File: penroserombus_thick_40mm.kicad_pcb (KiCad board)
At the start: 2 copper layers, 52.4 x 38 mm, 13 parts, among them J1 Conn_01x03_Female, J2 Conn_01x03_Female, J3 Conn_01x03_Male, J4 Conn_01x03_Male, SW1 SW_DPDT_x2

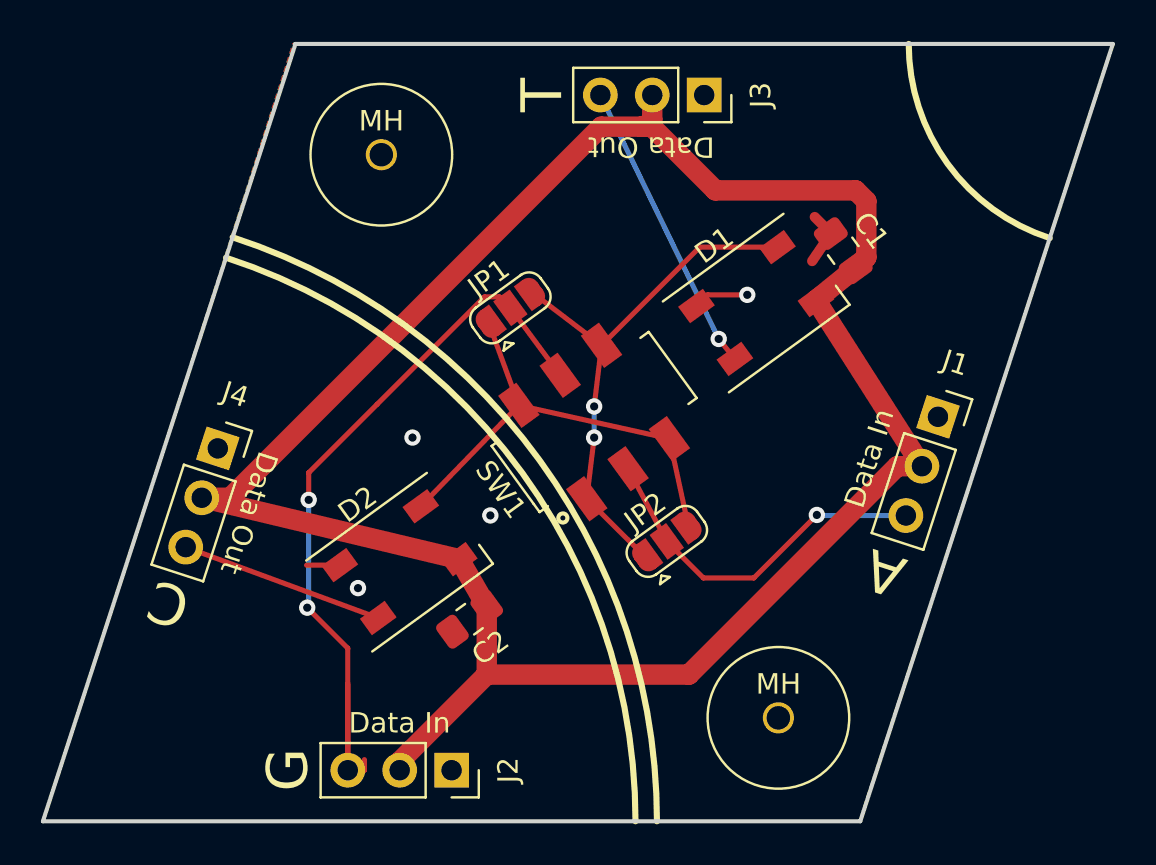
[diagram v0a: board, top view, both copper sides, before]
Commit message: added more mounting holes and generated gerbers
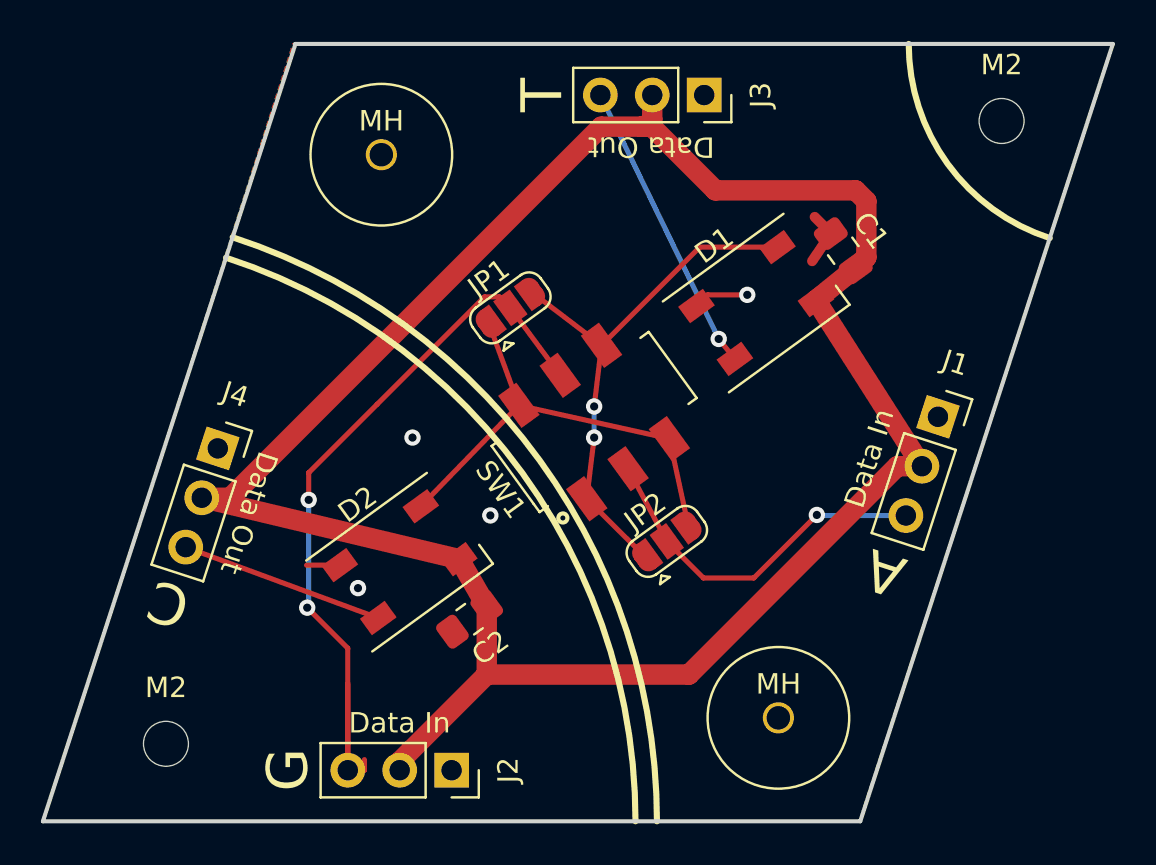
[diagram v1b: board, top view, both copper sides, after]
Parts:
- added M2: MountingHole_2.2mm_M2_ISO7380, MountingHole:MountingHole_2.2mm_M2_ISO7380, F.Cu at (126.9, 110.2)
- added M2: MountingHole_2.2mm_M2_ISO7380, MountingHole:MountingHole_2.2mm_M2_ISO7380, F.Cu at (167.8, 79.8)

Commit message: board has 4 leds instead of 2.
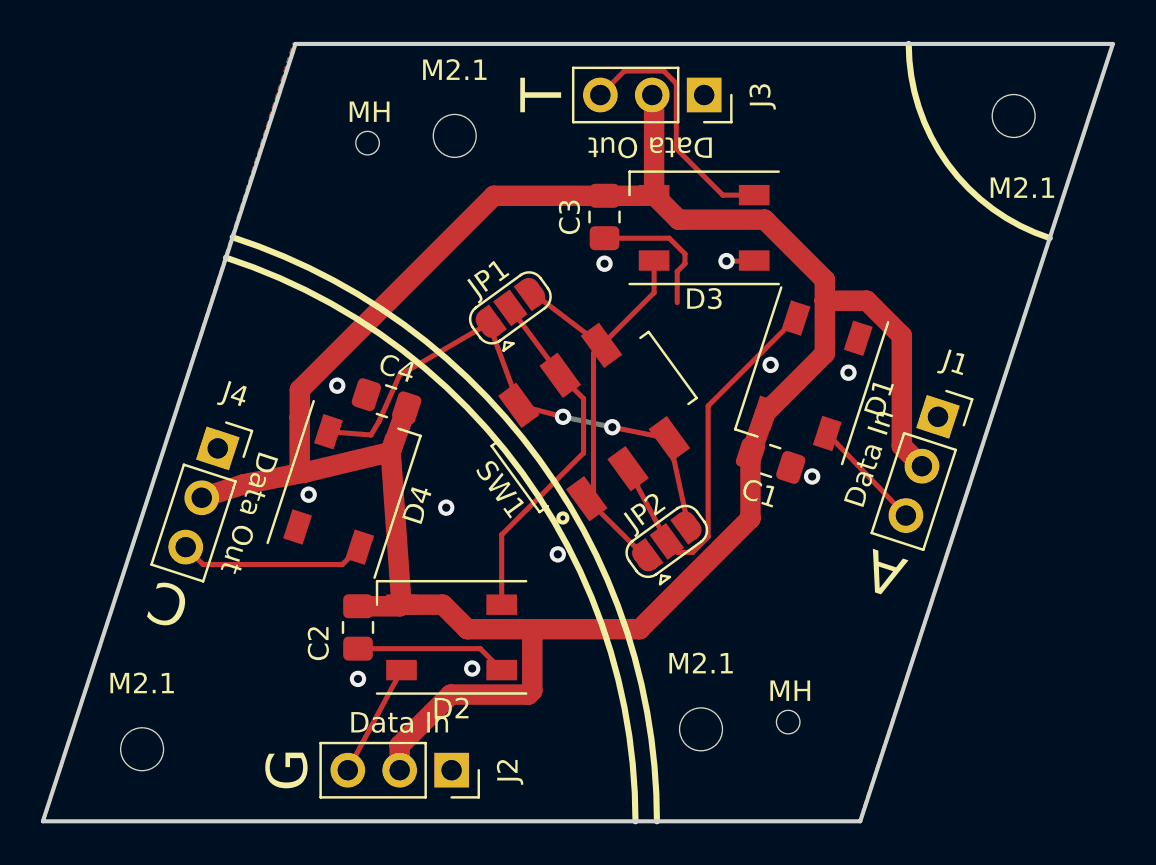
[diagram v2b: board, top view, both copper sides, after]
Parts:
- removed M2 (x2): MountingHole_2.2mm_M2_ISO7380, MountingHole:MountingHole_2.2mm_M2_ISO7380
- removed the MH at (156.8, 109.0)
- removed the MH at (137.4, 81.4)
- added C3: C, Capacitor_SMD:C_0805_2012Metric_Pad1.18x1.45mm_HandSolder, F.Cu at (148.3, 84.5)
- added C4: C, Capacitor_SMD:C_0805_2012Metric_Pad1.18x1.45mm_HandSolder, F.Cu at (137.7, 93.5)
- added D3: SK6812, LED_SMD:LED_SK6812_PLCC4_5.0x5.0mm_P3.2mm, F.Cu at (153.2, 85.0)
- added D4: SK6812, LED_SMD:LED_SK6812_PLCC4_5.0x5.0mm_P3.2mm, F.Cu at (135.6, 97.8)
- added M2.1: MountingHole_2.1mm, MountingHole:MountingHole_2.1mm, F.Cu at (141.0, 80.5)
- added M2.1: MountingHole_2.1mm, MountingHole:MountingHole_2.1mm, F.Cu at (168.4, 79.5)
- added M2.1: MountingHole_2.1mm, MountingHole:MountingHole_2.1mm, F.Cu at (153.1, 109.5)
- added M2.1: MountingHole_2.1mm, MountingHole:MountingHole_2.1mm, F.Cu at (125.7, 110.5)
- added MH: Pushpin_mountinghole, penroserombus:Pushpin_mountinghole, F.Cu at (157.3, 109.2)
- added MH: Pushpin_mountinghole, penroserombus:Pushpin_mountinghole, F.Cu at (136.7, 80.8)
- moved C1 10.9 mm to (156.5, 96.4), turned to 162 degrees
- moved C2 5.48 mm to (136.3, 104.5), turned to 90 degrees
- moved D1 4.48 mm to (158.5, 92.2), turned to 252 degrees
- moved D2 4.48 mm to (140.9, 105.0), turned to 180 degrees
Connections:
- J1 pad 3: Net-(J1-Pad3) -> Net-(D1-Pad2)
- J2 pad 3: Net-(J2-Pad3) -> Net-(D2-Pad2)
- J3 pad 3: Net-(D1-Pad4) -> Net-(D3-Pad4)
- J4 pad 3: Net-(D2-Pad4) -> Net-(D4-Pad4)
- JP1 pad 1: Net-(D2-Pad2) -> Net-(D4-Pad2)
- JP1 pad 2: Net-(J2-Pad3) -> Net-(D2-Pad4)
- JP1 pad 3: Net-(D1-Pad2) -> Net-(D3-Pad2)
- JP2 pad 1: Net-(D1-Pad2) -> Net-(D3-Pad2)
- JP2 pad 2: Net-(J1-Pad3) -> Net-(D1-Pad4)
- JP2 pad 3: Net-(D2-Pad2) -> Net-(D4-Pad2)
- SW1 pad 1: Net-(D1-Pad2) -> Net-(D3-Pad2)
- SW1 pad 2: Net-(J1-Pad3) -> Net-(D1-Pad4)
- SW1 pad 3: Net-(D2-Pad2) -> Net-(D4-Pad2)
- SW1 pad 4: Net-(D2-Pad2) -> Net-(D4-Pad2)
- SW1 pad 5: Net-(J2-Pad3) -> Net-(D2-Pad4)
- SW1 pad 6: Net-(D1-Pad2) -> Net-(D3-Pad2)
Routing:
- net Net-(J2-Pad3): track 39.3 -> 0.00 mm, vias 2 -> 0
- net Net-(D4-Pad2): track 0.00 -> 26.6 mm, vias 0 -> 2
- net Net-(D3-Pad2): track 0.00 -> 21.4 mm
- net Net-(D1-Pad2): track 26.5 -> 5.56 mm, vias 2 -> 0
- net Net-(J1-Pad3): track 17.8 -> 0.00 mm, vias 1 -> 0
- net Net-(D2-Pad2): track 23.1 -> 5.56 mm
- net Net-(D3-Pad4): track 0.00 -> 12.4 mm
- net Net-(D4-Pad4): track 0.00 -> 9.22 mm
- net GND: track 6.94 -> 15.6 mm, vias 4 -> 11
- net VCC: track 110.0 -> 118.3 mm
- net Net-(D2-Pad4): track 10.0 -> 17.5 mm
- net Net-(D1-Pad4): track 14.5 -> 19.1 mm, vias 1 -> 0

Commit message: fixed led 4 orientation
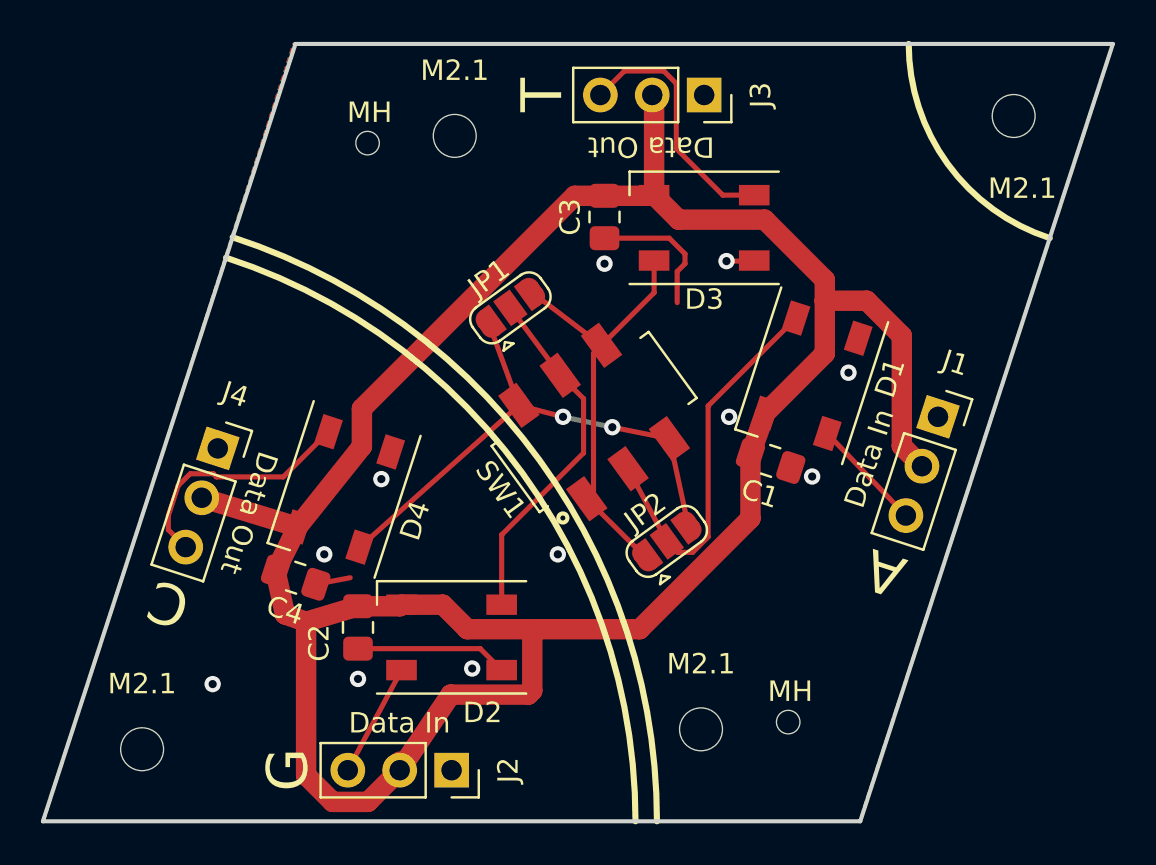
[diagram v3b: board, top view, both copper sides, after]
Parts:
- moved C4 9.71 mm to (133.2, 102.1), turned to 162 degrees
- turned D4 to 252 degrees
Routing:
- net VCC: track 118.3 -> 125.3 mm
- net Net-(D4-Pad4): track 9.22 -> 12.0 mm
- net GND: track 15.6 -> 17.3 mm

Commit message: rearranged leds a bit.
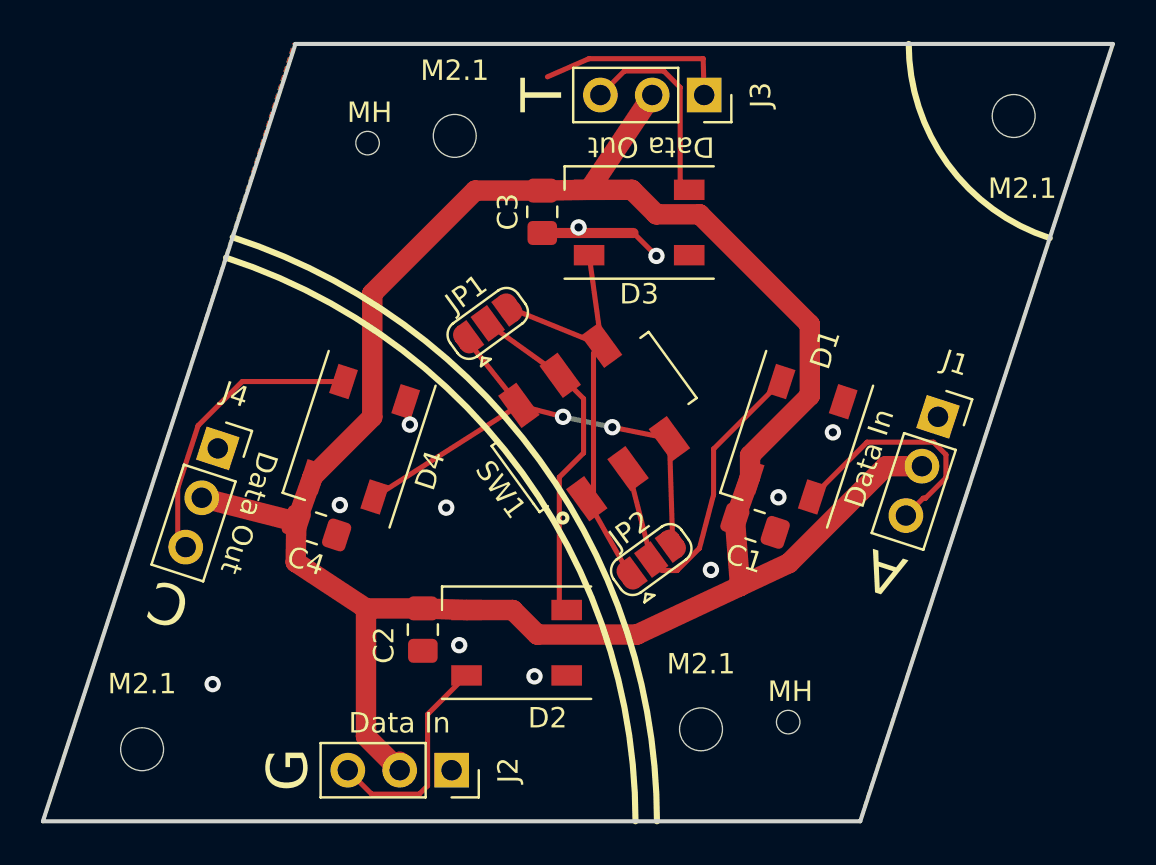
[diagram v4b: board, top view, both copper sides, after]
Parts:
- moved C1 3.27 mm to (155.7, 99.6)
- moved D3 3.19 mm to (150.0, 84.7)
- moved D2 3.19 mm to (144.0, 105.3)
- moved D1 3.19 mm to (157.7, 95.3)
- moved C2 3.18 mm to (139.4, 104.6)
- moved C3 3.06 mm to (145.3, 84.2)
- moved C4 2.62 mm to (134.2, 99.7)
- moved D4 2.56 mm to (136.3, 95.3)
- moved JP1 1.34 mm to (142.6, 89.7)
- moved JP2 1.17 mm to (150.6, 101.2)
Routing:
- net VCC: track 125.3 -> 108.8 mm
- net Net-(D1-Pad2): track 5.56 -> 11.8 mm
- net Net-(D2-Pad2): track 5.56 -> 10.8 mm
- net Net-(D3-Pad4): track 12.4 -> 9.92 mm
- net Net-(D4-Pad4): track 12.0 -> 14.3 mm
- net Net-(D1-Pad4): track 19.1 -> 17.2 mm
- net GND: track 17.3 -> 15.6 mm
- net Net-(D4-Pad2): track 26.6 -> 25.2 mm
- net Net-(D2-Pad4): track 17.5 -> 17.0 mm

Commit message: made gerbers
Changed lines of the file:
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@@
       (effects (font (size 0.5 0.5) (thickness 0.08)))
     )
-    (pad 1 smd roundrect (at -1.0375 0 162) (size 1.175 1.45) (layers F.Cu F.Paste F.Mask) (roundrect_rratio 0.212766)
-      (net 2 GND))
-    (pad 2 smd roundrect (at 1.0375 0 162) (size 1.175 1.45) (layers F.Cu F.Paste F.Mask) (roundrect_rratio 0.212766)
+    (pad 1 smd roundrect (at -1.0375 0 162) (size 1.175 1.45) (layers F.Cu F.Paste F.Mask) (roundrect_rratio 0.2127659574468085)
+      (net 2 GND))
+    (pad 2 smd roundrect (at 1.0375 0 162) (size 1.175 1.45) (layers F.Cu F.Paste F.Mask) (roundrect_rratio 0.2127659574468085)
       (net 1 VCC))
     (model ${KISYS3DMOD}/Capacitor_SMD.3dshapes/C_0805_2012Metric.wrl
@@
       (effects (font (size 0.5 0.5) (thickness 0.08)))
     )
-    (pad 2 smd roundrect (at 1.0375 0 90) (size 1.175 1.45) (layers F.Cu F.Paste F.Mask) (roundrect_rratio 0.212766)
-      (net 1 VCC))
-    (pad 1 smd roundrect (at -1.0375 0 90) (size 1.175 1.45) (layers F.Cu F.Paste F.Mask) (roundrect_rratio 0.212766)
+    (pad 2 smd roundrect (at 1.0375 0 90) (size 1.175 1.45) (layers F.Cu F.Paste F.Mask) (roundrect_rratio 0.2127659574468085)
+      (net 1 VCC))
+    (pad 1 smd roundrect (at -1.0375 0 90) (size 1.175 1.45) (layers F.Cu F.Paste F.Mask) (roundrect_rratio 0.2127659574468085)
       (net 2 GND))
     (model ${KISYS3DMOD}/Capacitor_SMD.3dshapes/C_0805_2012Metric.wrl
@@
   (via (at 140.589 98.679) (size 0.8) (drill 0.4) (layers F.Cu B.Cu) (net 2))
   (via (at 141.224 105.41) (size 0.8) (drill 0.4) (layers F.Cu B.Cu) (net 2))
-  (via (at 138.811 94.615) (size 0.8) (drill 0.4) (layers F.Cu B.Cu) (net 2))
+  (via (at 138.176 94.996) (size 0.8) (drill 0.4) (layers F.Cu B.Cu) (net 2))
   (via (at 135.382 98.552) (size 0.8) (drill 0.4) (layers F.Cu B.Cu) (net 2))
   (via (at 144.907 106.934) (size 0.8) (drill 0.4) (layers F.Cu B.Cu) (net 2))

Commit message: small tweaks to traces
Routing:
- net VCC: track 108.8 -> 107.9 mm
- net GND: vias 11 -> 10

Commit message: added kite and dart tiling
idk why im doing this
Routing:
- net GND: track 15.6 -> 25.8 mm, vias 10 -> 9
- net Net-(D1-Pad2): track 11.7 -> 4.67 mm
- net VCC: track 107.9 -> 102.0 mm
